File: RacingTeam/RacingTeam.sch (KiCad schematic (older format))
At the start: 82 parts, among them J1 BusIn, J10 BatteryIn, J11 ShutdownIn, J2 TestPoint, J3 TestPoint, J4 TestPin, J5 TestPin, J6 PreCharge Relay Out, J7 AIROut, J8 Discharge Relay Out, J9 PCB OUT, Q1 TP0610T, Q2 2N7002, Q3 2N7002, Q4 2N7002, Q5 2N7002, Q6 TP0610T, Q7 2N7002, Q8 TP0610T, U1 LM311, U2 LM311, U3 4N35, U6 NE555D

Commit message: Update 2N7002H6327XTSA2.kicad_mod, 4N35SM.kicad_mod, and 69 more files...
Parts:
- removed D7: D, GRC2022:SD0805S040S0R5, symbol RacingTeamPCB:D
- removed F3: Fuse_Small, GRC2022:FUSE_0154004.DRTL, symbol Device:Fuse_Small
- removed Q4: 2N7002, GRC2022:TRANS_MMBT2907A, symbol RacingTeamPCB:2N7000
- added C10, C9: 1μF, GRC2022:C_0603, symbol RacingTeamPCB:C
- added Q4: TP0610T, GRC2022:SOT95P280X100-6N, symbol RacingTeamPCB:TP0610T
- added U4: MC78M12ABDTRKG, GRC2022:TO229P990X238-4N, symbol RacingTeamPCB:MC78M12ABDTRKG
- J2: value TestPoint -> Bypass Pin
- J3: value TestPoint -> BypassPin
- J4, J5: value TestPin -> BypassPin
- J6: value PreCharge Relay Out -> PC Relay
- J9: value PCB OUT -> Molex
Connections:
- net labels added: +BATT, -BATT, AIRON, PreChargeON
- net labels removed: AIROn, AIROut, Ec3Out+, PreChargeOn, Shutdown+, Shutdown-, VCC
- wire segments 186 -> 207
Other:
- note added: "12V+ - High Voltage Regulated 12V (From HV Regulator)\nGND - High Voltage Regulated Isolated Ground (From HV Regulator)\n+BATT - Unregulated Battery Supply +\n-BATT - Unregulated Battery Supply - (Synced to GLV-)\nGLV+ - Grounded Low Voltage + (from GLV Regulator)\nGLV- - Grounded Low Voltage - (From GLV Regulator)"
- note added: "ConnectorsOut\n\n\n"
- note added: "GLV Regulator\n\n\n"
- note added: "GLV\n\n"
- note added: "HV\n"
- note added: "Power Symbol Definitions\n"
- note added: "Schematic Notes\n\n\n"
- note added: "The EC3SAW provides isloated 12V from the GLV to the HV side to power any components on the HV side as well as\nprovide the reference voltages for Voltage Divider Circuits\n"
- note added: "The Enable Pin on the isolated HV GLV Regulator is controlled via the Shutdown Circuit, if the Shutdown Circuit is not active,\nno HV components will power on, but the GLV side will still remain on \n(From Battery to GLV regulator) to display a Green light indicating safe voltages present\ninside the accumulator\n"
- note removed: "12V+ - Unconverted 12V from Battery\nVCC - Diode Filtered GLV+\nGLV+ - Grounded Low Voltage +\nGLV- - Grounded Low Voltage -"
- note removed: "Input from battery on GLV side\n\n"
- note removed: "Voltage Regulation\n"
- moved on the sheet: C1, C2, C3, C4, C5, C6, C8, D1, D2, D3, D4, D5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

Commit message: Update GRC22Footprints.mod, C_0603_1608Metric.step, and 19 more files...
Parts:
- C1, C10, C3, C4, C5, C6, C8, C9: footprint GRC2022:C_0603 -> GRC22Footprints:C_0603_1608Metric_Pad1.08x0.95mm_HandSolder; symbol RacingTeamPCB:C -> GRC22Symbols:C
- C2: footprint GRC2022:C_0603 -> GRC22Footprints:C_0603_1608Metric_Pad1.08x0.95mm_HandSolder
- D1, D2: footprint GRC2022:SOD57-10 -> GRC22Footprints:SOD57-10; symbol RacingTeamPCB:D_Zener -> GRC22Symbols:D
- D3, D4, D5: footprint GRC2022:SD0805S040S0R5 -> GRC22Footprints:D_0805_2012Metric_Castellated
- D6, D8: footprint GRC2022:SunLED -> GRC22Footprints:D_0603_1608Metric_Castellated; symbol RacingTeamPCB:LED -> GRC22Symbols:D
- F1, F2, F5, F6: footprint GRC2022:FUSE_0154004.DRTL -> GRC22Footprints:FUSE_0154004.DRTL
- J1: footprint GRC2022:TE_8PCV-02-006 -> GRC22Footprints:TE_8PCV-02-006
- J10, J11, J6, J7, J8: footprint GRC2022:CUI_TBL001-500-02GY-2GY -> GRC22Footprints:CUI_TBL001-500-02GY-2GY
- J2, J3, J4, J5: footprint GRC2022:SinglePinHeader -> GRC22Footprints:PinHeader_1x01_P2.54mm_Vertical
- J9: footprint GRC2022:Molex -> GRC22Footprints:Molex; symbol RacingTeamPCB:Conn_01x06 -> GRC22Symbols:Conn_01x06
- JP1, JP2: footprint GRC2022:DualPinHeader -> GRC22Footprints:PinHeader_1x02_P2.54mm_Vertical; symbol RacingTeamPCB:Jumper -> GRC22Symbols:Jumper
- PS1: footprint GRC2022:EC3SAW-24S12P -> GRC22Footprints:EC3SAW-24S12P; symbol RacingTeamPCB:EC3SAW-24S12P -> GRC22Symbols:EC3SAW-24S12P
- Q1, Q4, Q6, Q8: footprint GRC2022:SOT95P280X100-6N -> GRC22Footprints:2N7002H6327XTSA2_v2; symbol RacingTeamPCB:TP0610T -> GRC22Symbols:RSC002P03T316
- Q2, Q3, Q5, Q7: footprint GRC2022:TRANS_MMBT2907A -> GRC22Footprints:2N7002H6327XTSA2; symbol RacingTeamPCB:2N7000 -> GRC22Symbols:2N7002
- R1, R16, R17, R18, R19, R2, R20, R22, R24, R26, R27, R28, R29, R3, R30, R31, R32: footprint GRC2022:R_0603 -> GRC22Footprints:R_0603_1608Metric_Pad0.98x0.95mm_HandSolder; symbol RacingTeamPCB:R -> GRC22Symbols:R
- R10, R11, R8, R9: footprint GRC2022:R_0805 -> GRC22Footprints:R_0805_2012Metric_Pad1.20x1.40mm_HandSolder
- R12, R13, R14, R15, R33, R34, R35, R36, R6, R7: footprint GRC2022:R_0805 -> GRC22Footprints:R_0805_2012Metric_Pad1.20x1.40mm_HandSolder; symbol RacingTeamPCB:R -> GRC22Symbols:R
- R21, R23, R25: footprint GRC2022:R_0603 -> GRC22Footprints:R_0805_2012Metric_Pad1.20x1.40mm_HandSolder; symbol RacingTeamPCB:R -> GRC22Symbols:R
- R4, R5: footprint GRC2022:R_0603 -> GRC22Footprints:R_0603_1608Metric_Pad0.98x0.95mm_HandSolder
- U1: footprint GRC2022:SOP65P640X120-8N -> GRC22Footprints:LM311PW; symbol Comparator:LM311 -> GRC22Symbols:LM311
- U2: footprint GRC2022:SOP65P640X120-8N -> GRC22Footprints:LM311PW; symbol RacingTeamPCB:LM311 -> GRC22Symbols:LM311
- U3: footprint GRC2022:OPTO_4N35SM -> GRC22Footprints:OPTO_4N35SM; symbol RacingTeamPCB:4N35 -> GRC22Symbols:4N35SM
- U4: footprint GRC2022:TO229P990X238-4N -> GRC22Footprints:TO229P990X238-4N; symbol RacingTeamPCB:MC78M12ABDTRKG -> GRC22Symbols:MC78M12ABDTRKG
- U6: footprint GRC2022:NE555PSRE4 -> GRC22Footprints:NE555PSRE4; symbol RacingTeamPCB:NE555D -> GRC22Symbols:NE555D
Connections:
- net 555Output: now also Q7.1 (G); no longer Q7.2 (G)
- net DischargeIn: now also Q3.2 (S); no longer Q3.1 (S)
- net GLV-: now also J9.3 (Pin_3), Q5.2 (S), Q7.2 (S); no longer J9.4 (Pin_4), Q5.1 (S), Q7.1 (S)
- net InvertBus: no longer Q5.2 (G), R26.1, U3.4
- net PreChargeON: now also Q3.1 (G); no longer Q3.2 (G)
- net PrechargeCompOUT: now also Q2.1 (G); no longer Q2.2 (G)
- net RED+: now also J9.4 (Pin_4); no longer J9.3 (Pin_3)
- net at R23.2: now also Q2.2 (S); no longer Q2.1 (S)
- new net: Q5.1 (G), R26.1, U3.4
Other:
- moved on the sheet: R20, R26

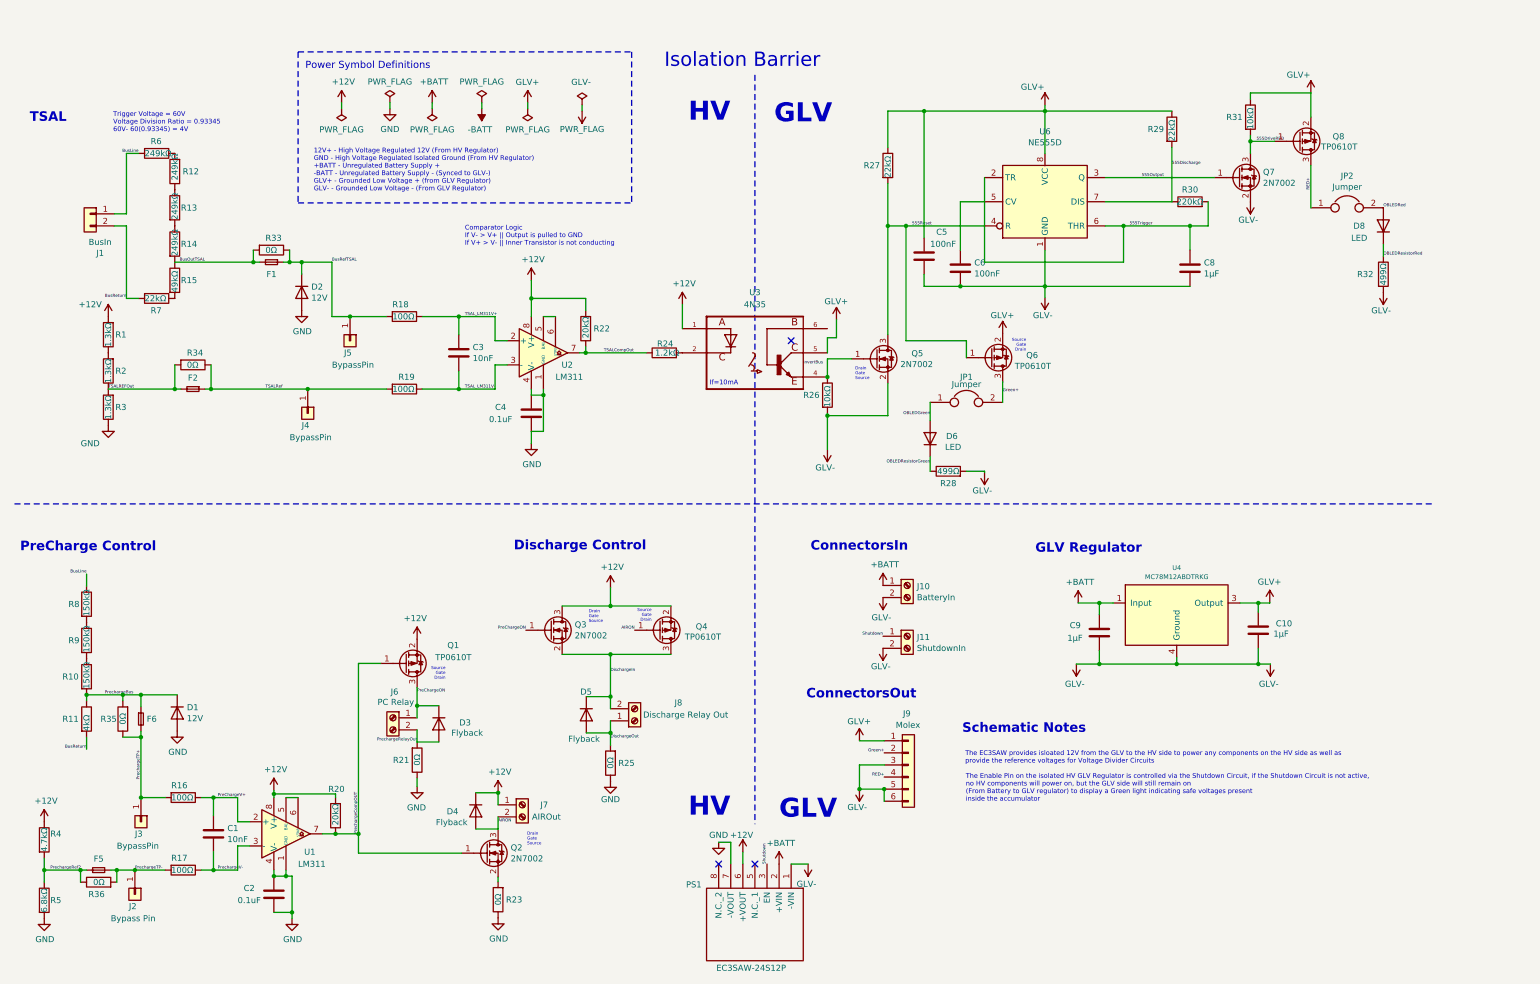
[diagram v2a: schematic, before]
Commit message: Update GRC22Footprints.mod, CONV_SPBW06F-12.kicad_mod, and 43 more files...
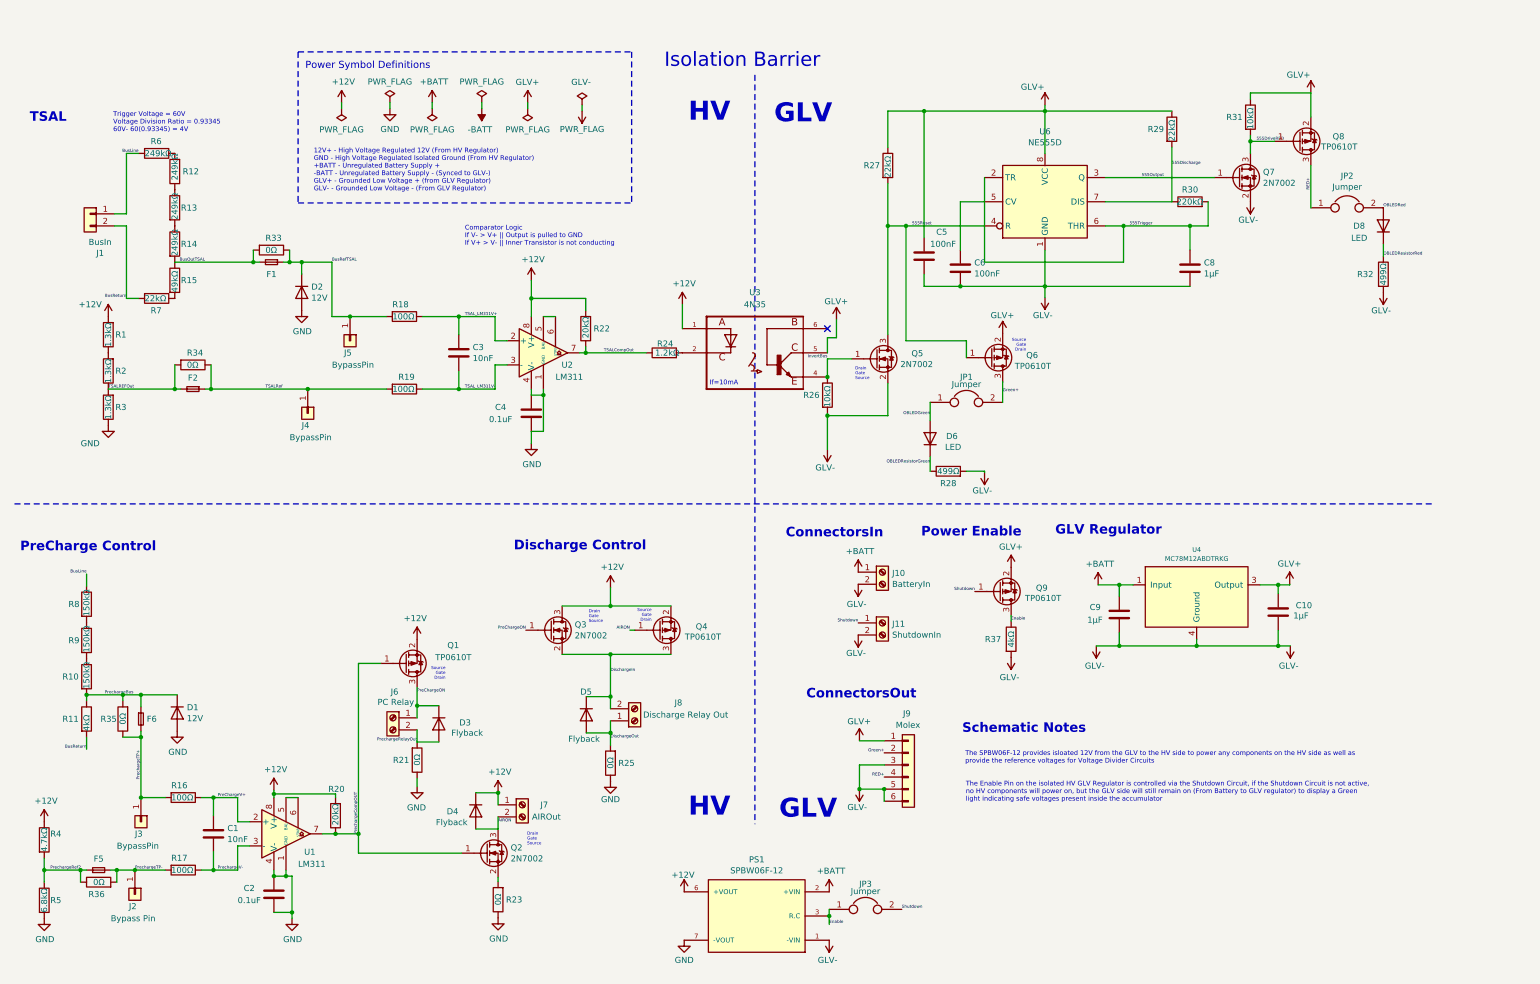
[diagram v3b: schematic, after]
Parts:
- removed PS1: EC3SAW-24S12P, GRC22Footprints:EC3SAW-24S12P, symbol GRC22Symbols:EC3SAW-24S12P
- added JP3: Jumper, GRC22Footprints:PinHeader_1x02_P2.54mm_Vertical, symbol GRC22Symbols:Jumper
- added PS1: SPBW06F-12, GRC22Footprints:CONV_SPBW06F-12, symbol GRC22Symbols:SPBW06F-12
- added Q9: TP0610T, GRC22Footprints:2N7002H6327XTSA2_v2, symbol GRC22Symbols:RSC002P03T316
- added R37: 4kΩ, GRC22Footprints:R_0603_1608Metric_Pad0.98x0.95mm_HandSolder, symbol GRC22Symbols:R
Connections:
- net +12V: now also PS1.6 (+VOUT)
- net +BATT: now also PS1.2 (+VIN)
- net GLV+: now also Q9.2 (S)
- net GLV-: now also PS1.1 (-VIN), R37.2
- net GND: now also PS1.7 (-VOUT)
- net InvertBus: now also Q5.1 (G), R26.1, U3.4
- net Shutdown: now also JP3.2, Q9.1 (G)
- new net Enable: JP3.1, PS1.3 (R.C), Q9.3 (D), R37.1
- no-connect marks 3 -> 1
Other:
- note added: "Power Enable\n\n\n"
- note added: "The Enable Pin on the isolated HV GLV Regulator is controlled via the Shutdown Circuit, if the Shutdown Circuit is not active,\nno HV components will power on, but the GLV side will still remain on (From Battery to GLV regulator) to display a Green\nlight indicating safe voltages present inside the accumulator\n"
- note added: "The SPBW06F-12 provides isloated 12V from the GLV to the HV side to power any components on the HV side as well as\nprovide the reference voltages for Voltage Divider Circuits\n"
- note removed: "The EC3SAW provides isloated 12V from the GLV to the HV side to power any components on the HV side as well as\nprovide the reference voltages for Voltage Divider Circuits\n"
- note removed: "The Enable Pin on the isolated HV GLV Regulator is controlled via the Shutdown Circuit, if the Shutdown Circuit is not active,\nno HV components will power on, but the GLV side will still remain on \n(From Battery to GLV regulator) to display a Green light indicating safe voltages present\ninside the accumulator\n"
- moved on the sheet: C10, C9, J10, J11, U4
